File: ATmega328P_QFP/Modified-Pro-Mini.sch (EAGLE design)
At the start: 25 parts, among them Q1 8/16/20MHz, U1 ATMEGA328, U2 MIC5205

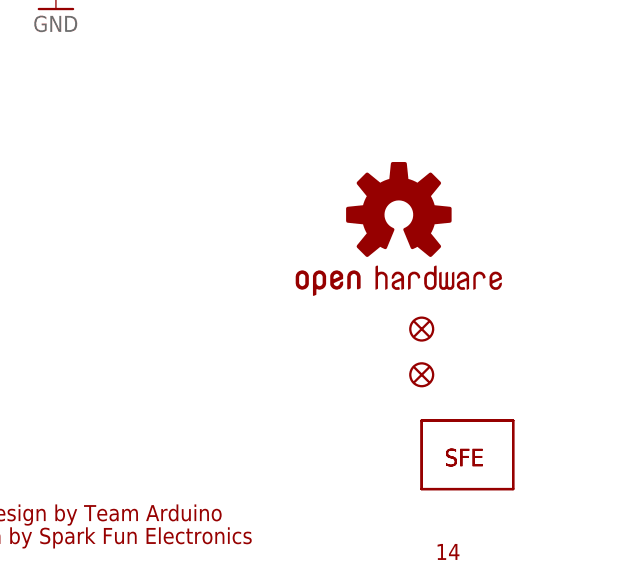
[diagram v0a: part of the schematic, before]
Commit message: updated silk
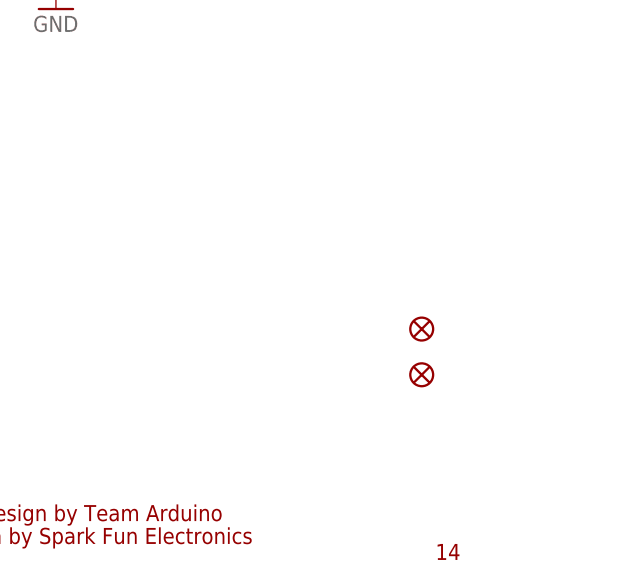
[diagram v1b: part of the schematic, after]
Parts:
- removed U$1: LOGO-SFESK, SparkFun:LOGO-SFESK
- removed U$11: LOGO-SFENEW, SparkFun:LOGO-SFENEW
- removed U$3: OSHW-LOGOS, SparkFun:OSHW-LOGOS
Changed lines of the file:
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@@
 <part name="D3" library="Testing" deviceset="LED" device="" value="Green"/>
 <part name="GND8" library="SparkFun" deviceset="GND" device=""/>
-<part name="U$11" library="SparkFun" deviceset="LOGO-SFE" device="NEW"/>
 <part name="U2" library="SparkFun" deviceset="V_REG_LDO" device="SMD" value="MIC5205"/>
 <part name="C19" library="SparkFun" deviceset="CAP_POL" device="1206" value="10uF"/>
@@
 <part name="JP6" library="SparkFun" deviceset="M12" device="PTH" value=""/>
 <part name="JP7" library="SparkFun" deviceset="M12" device="PTH" value=""/>
-<part name="U$1" library="SparkFun" deviceset="LOGO-SFE" device="SK"/>
 <part name="GND4" library="SparkFun" deviceset="GND" device=""/>
 <part name="JP2" library="SparkFun" deviceset="M02" device="PTH"/>
@@
 <part name="GND5" library="SparkFun" deviceset="GND" device=""/>
 <part name="JP1" library="SparkFun" deviceset="ARDUINO_SERIAL_PROGRAM" device="PTH" value="FTDI Basic"/>
-<part name="U$3" library="SparkFun" deviceset="OSHW-LOGO" device="S"/>
 <part name="R1" library="SparkFun" deviceset="RESISTOR" device="0603-RES"/>
 <part name="R3" library="SparkFun" deviceset="RESISTOR" device="0603-RES"/>
@@
 </instance>
 <instance part="GND8" gate="1" x="198.12" y="68.58"/>
-<instance part="U$11" gate="G$1" x="241.3" y="17.78"/>
 <instance part="U2" gate="G$1" x="45.72" y="157.48"/>
 <instance part="C19" gate="G$1" x="22.86" y="157.48"/>
@@
 <instance part="JP6" gate="G$1" x="106.68" y="83.82" rot="R180"/>
 <instance part="JP7" gate="G$1" x="55.88" y="86.36"/>
-<instance part="U$1" gate="G$1" x="241.3" y="17.78"/>
 <instance part="GND4" gate="1" x="134.62" y="119.38"/>
 <instance part="JP2" gate="G$1" x="73.66" y="43.18" rot="R180"/>
@@
 <instance part="GND5" gate="1" x="144.78" y="93.98"/>
 <instance part="JP1" gate="G$1" x="22.86" y="83.82"/>
-<instance part="U$3" gate="G$1" x="236.22" y="45.72"/>
 <instance part="R1" gate="G$1" x="223.52" y="152.4" rot="R90"/>
 <instance part="R3" gate="G$1" x="231.14" y="149.86" rot="R90"/>

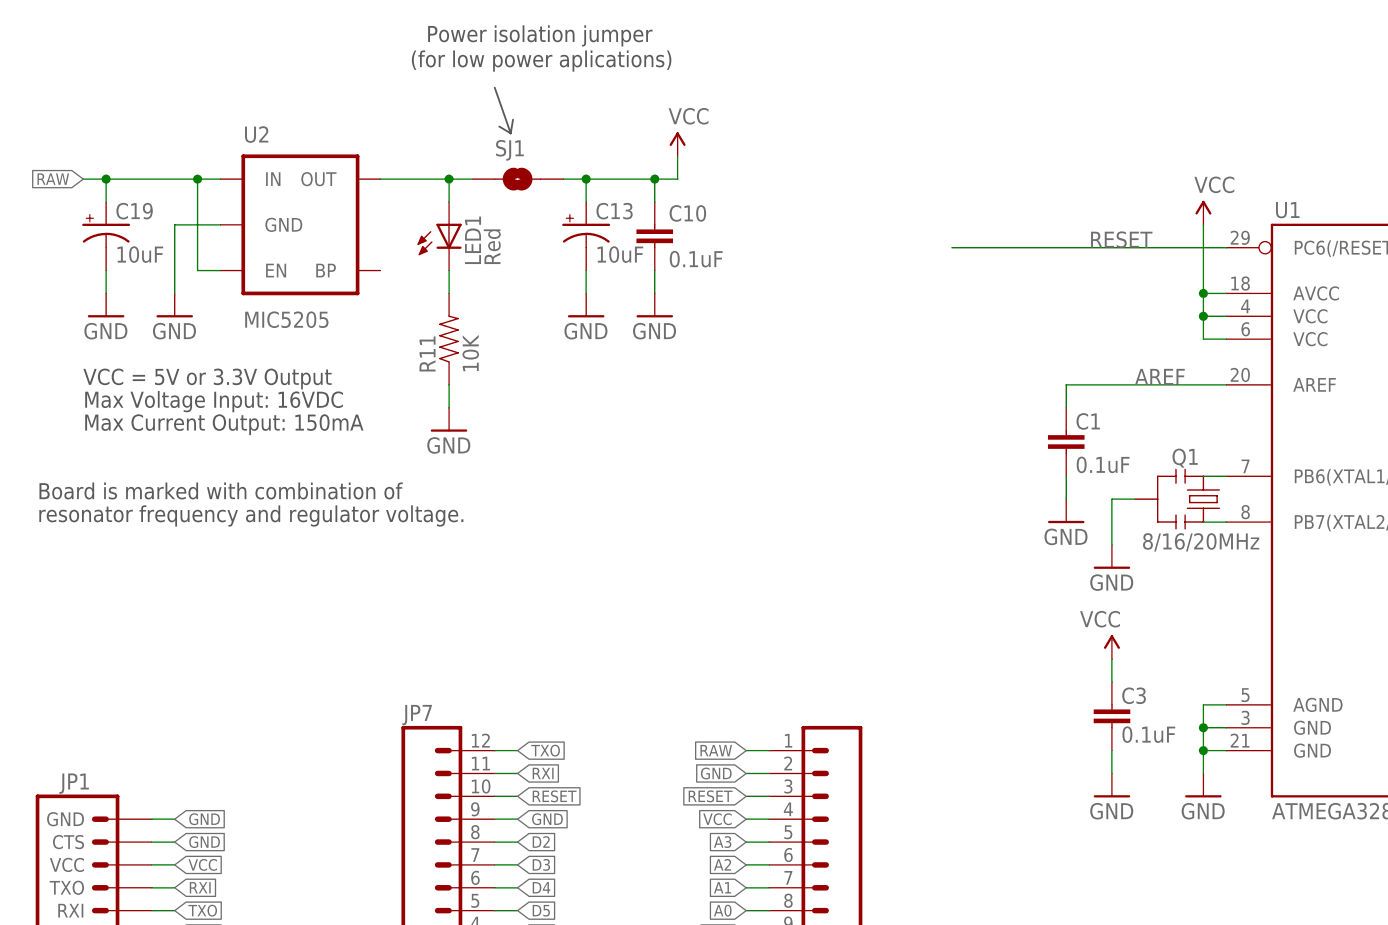
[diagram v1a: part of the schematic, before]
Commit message: removed power regulator
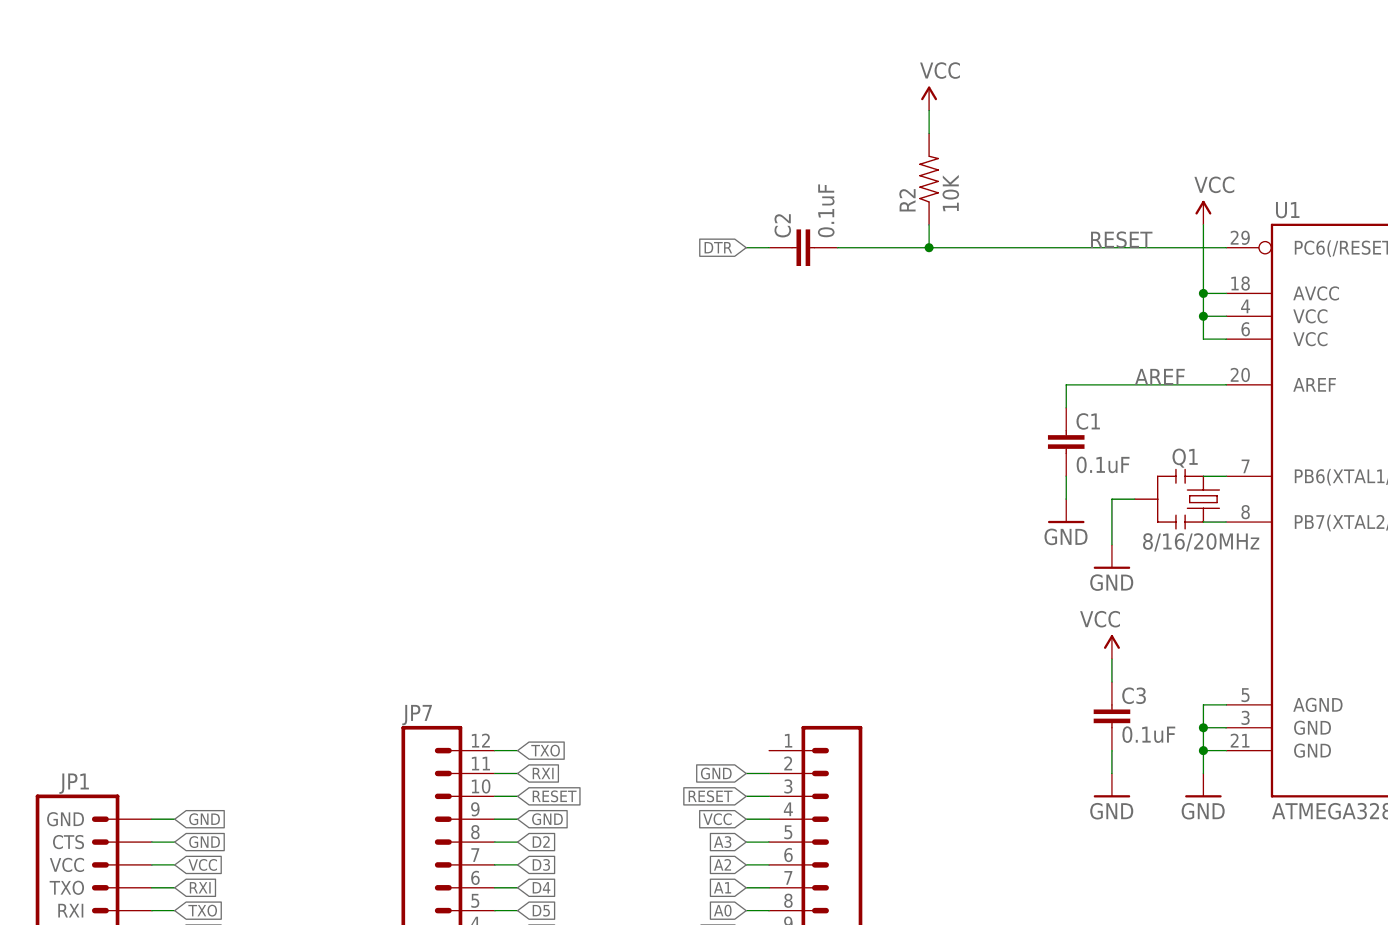
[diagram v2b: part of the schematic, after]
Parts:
- removed C10: 0.1uF, SparkFun:CAP0603-CAP
- removed C13, C19: 10uF, SparkFun:CAP_POL1206
- removed LED1: Red, Testing:LED
- removed R11: 10K, SparkFun:RESISTOR0603-RES
- removed SJ1: SOLDERJUMPERNC, SparkFun-Passives:SOLDERJUMPERNC
- removed U2: MIC5205, SparkFun:V_REG_LDOSMD
- added C2: 0.1uF, SparkFun:CAP0603-CAP
- added R2: 10K, SparkFun:RESISTOR0603-RES
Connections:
- removed net N$3: LED1.A, SJ1.1, U2.OUT
- removed net N$4: LED1.C, R11.2
- removed net RAW: C19.+, JP6.1, U2.EN, U2.IN
- net DTR: now also C2.2
- net GND: no longer C10.2, C13.-, C19.-, R11.1, U2.GND
- net RESET: now also C2.1, R2.1
- net VCC: now also R2.2; no longer C10.1, C13.+, SJ1.2
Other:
- note removed: "(for low power aplications)"
- note removed: "Board is marked with combination of"
- note removed: "Max Current Output: 150mA"
- note removed: "Max Voltage Input: 16VDC"
- note removed: "Power isolation jumper"
- note removed: "VCC = 5V or 3.3V Output"
- note removed: "resonator frequency and regulator voltage."

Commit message: changed raw pin to gnd
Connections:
- net GND: now also JP6.1
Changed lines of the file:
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@@
 <pinref part="JP6" gate="G$1" pin="2"/>
 <label x="93.98" y="96.52" size="1.27" layer="95" rot="R180" xref="yes"/>
+<pinref part="JP6" gate="G$1" pin="1"/>
+<wire x1="96.52" y1="99.06" x2="93.98" y2="99.06" width="0.1524" layer="91"/>
+<wire x1="93.98" y1="99.06" x2="93.98" y2="96.52" width="0.1524" layer="91"/>
 </segment>
 <segment>

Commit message: added decoupling cap
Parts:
- added C13: 10uF, SparkFun:CAP_POL1206
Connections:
- net GND: now also C13.-
- net VCC: now also C13.+
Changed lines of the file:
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@@
 <part name="P+11" library="SparkFun" deviceset="3.3V" device="" value="VCC"/>
 <part name="C2" library="SparkFun" deviceset="CAP" device="0603-CAP" value="0.1uF"/>
+<part name="C13" library="SparkFun" deviceset="CAP_POL" device="1206" value="10uF"/>
+<part name="GND25" library="SparkFun" deviceset="GND" device=""/>
 </parts>
 <sheets>
@@
 <attribute name="VALUE" x="103.759" y="155.956" size="1.778" layer="96" rot="R90"/>
 </instance>
+<instance part="C13" gate="G$1" x="93.98" y="132.08"/>
+<instance part="GND25" gate="1" x="93.98" y="121.92"/>
 </instances>
 <busses>
@@
 <label x="30.48" y="91.44" size="1.27" layer="95" xref="yes"/>
 </segment>
+<segment>
+<wire x1="93.98" y1="124.46" x2="93.98" y2="127" width="0.1524" layer="91"/>
+<pinref part="C13" gate="G$1" pin="-"/>
+<pinref part="GND25" gate="1" pin="GND"/>
+</segment>
 </net>
 <net name="AREF" class="0">
@@
 <pinref part="P+11" gate="G$1" pin="3.3V"/>
 </segment>
-</net>
+<segment>
+<pinref part="C13" gate="G$1" pin="+"/>
+<wire x1="93.98" y1="134.62" x2="93.98" y2="137.16" width="0.1524" layer="91"/>
+<label x="93.98" y="137.16" size="1.778" layer="95" rot="R90"/>
+</segment>
+</net>

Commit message: added decoupling cap
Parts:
- added C4: 0.1uF, SparkFun:CAP0603-CAP
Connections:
- net GND: now also C4.1
- net VCC: now also C4.2
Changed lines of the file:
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@@
 <part name="C13" library="SparkFun" deviceset="CAP_POL" device="1206" value="10uF"/>
 <part name="GND25" library="SparkFun" deviceset="GND" device=""/>
+<part name="C4" library="SparkFun" deviceset="CAP" device="0603-CAP" value="0.1uF"/>
+<part name="GND2" library="SparkFun" deviceset="GND" device=""/>
 </parts>
 <sheets>
@@
 <instance part="C13" gate="G$1" x="93.98" y="132.08"/>
 <instance part="GND25" gate="1" x="93.98" y="121.92"/>
+<instance part="C4" gate="G$1" x="104.14" y="132.08" smashed="yes" rot="R180">
+<attribute name="NAME" x="105.156" y="132.207" size="1.778" layer="95"/>
+<attribute name="VALUE" x="105.156" y="127.381" size="1.778" layer="96"/>
+</instance>
+<instance part="GND2" gate="1" x="104.14" y="121.92"/>
 </instances>
 <busses>
@@
 <pinref part="GND25" gate="1" pin="GND"/>
 </segment>
+<segment>
+<wire x1="104.14" y1="124.46" x2="104.14" y2="127" width="0.1524" layer="91"/>
+<pinref part="C4" gate="G$1" pin="1"/>
+<pinref part="GND2" gate="1" pin="GND"/>
+</segment>
 </net>
 <net name="AREF" class="0">
@@
 <label x="93.98" y="137.16" size="1.778" layer="95" rot="R90"/>
 </segment>
-</net>
+<segment>
+<pinref part="C4" gate="G$1" pin="2"/>
+<wire x1="104.14" y1="134.62" x2="104.14" y2="137.16" width="0.1524" layer="91"/>
+<label x="104.14" y="137.16" size="1.778" layer="95" rot="R90"/>
+</segment>
+</net>

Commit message: Prepare silkscreen layers for OSH Park printing (#4)
* Fix typo in bPlace layer
* Remove fiducials
* Cleared the tNames layer
* Slight adjustments to prevent text from overlapping copper
* got rid of kink in TXO line
* moved via slightly
* bottom silk tweak
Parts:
- removed JP5, JP8: FIDUCIALUFIDUCIAL, SparkFun:FIDUCIALUFIDUCIAL
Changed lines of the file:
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@@
 <part name="P+2" library="SparkFun" deviceset="3.3V" device="" value="VCC"/>
 <part name="P+3" library="SparkFun" deviceset="3.3V" device="" value="VCC"/>
-<part name="JP5" library="SparkFun" deviceset="FIDUCIAL" device="UFIDUCIAL"/>
-<part name="JP8" library="SparkFun" deviceset="FIDUCIAL" device="UFIDUCIAL"/>
 <part name="JP3" library="SparkFun" deviceset="M02" device="PTH"/>
 <part name="Q1" library="Testing" deviceset="RESONATOR" device="1:1" value="8/16/20MHz"/>
@@
 <instance part="P+2" gate="G$1" x="223.52" y="160.02"/>
 <instance part="P+3" gate="G$1" x="231.14" y="160.02"/>
-<instance part="JP5" gate="G$1" x="238.76" y="27.94"/>
-<instance part="JP8" gate="G$1" x="238.76" y="33.02"/>
 <instance part="JP3" gate="G$1" x="99.06" y="43.18" rot="R180"/>
 <instance part="Q1" gate="G$1" x="144.78" y="127" smashed="yes" rot="R270">

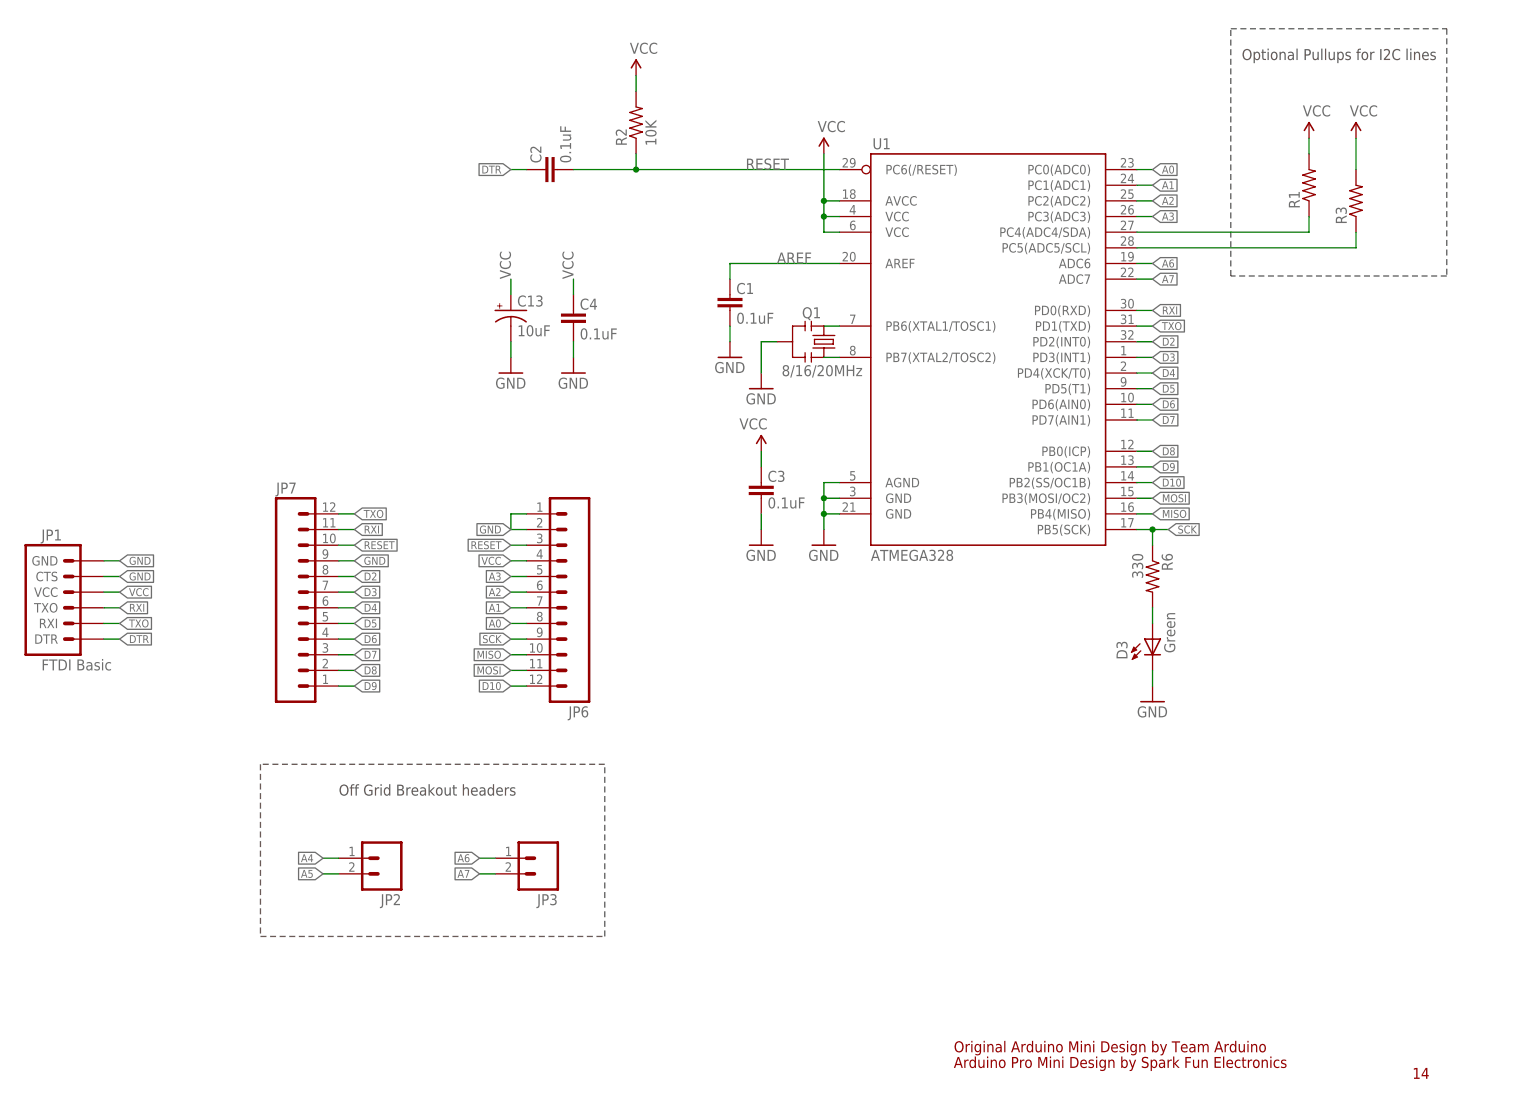
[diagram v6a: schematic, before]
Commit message: New board design: - larger footprint by the ICD requirements (no holes) - removed headers - added DF12 connector footprint
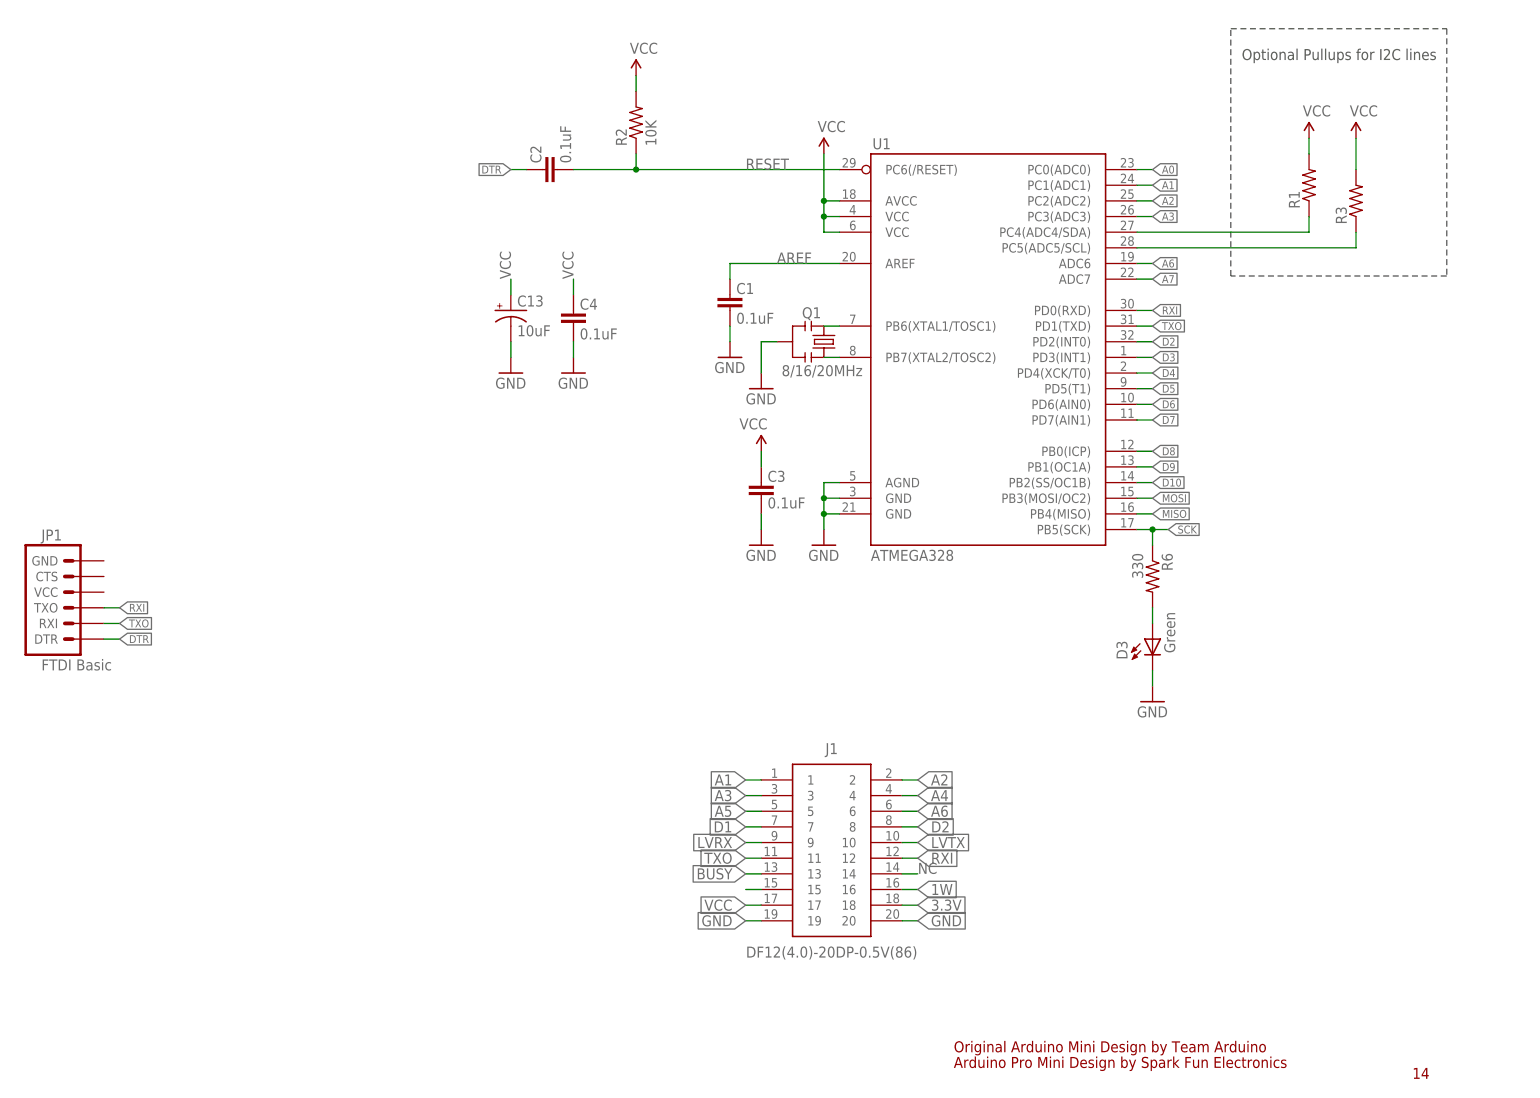
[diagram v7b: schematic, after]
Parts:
- removed JP2, JP3: (no value), SparkFun:M02PTH
- removed JP6, JP7: M12PTH, SparkFun:M12PTH
- added J1: DF12(4.0)-20DP-0.5V(86), DF12(4.0)-20DP-0.5V(86):DF12(4.0)-20DP-0.5V(86)
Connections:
- new net 1W: J1.16
- new net 3.3V: J1.18
- new net BUSY: J1.13
- new net D1: J1.7
- new net LVRX: J1.9
- new net LVTX: J1.10
- new net N$9: J1.15
- new net NC: J1.14
- net A0: no longer JP6.8
- net A1: now also J1.1; no longer JP6.7
- net A2: now also J1.2; no longer JP6.6
- net A3: now also J1.3; no longer JP6.5
- net A4: now also J1.4; no longer JP2.1
- net A5: now also J1.5; no longer JP2.2
- net A6: now also J1.6; no longer JP3.1
- net A7: no longer JP3.2
- net D10: no longer JP6.12
- net D2: now also J1.8; no longer JP7.8
- net D3: no longer JP7.7
- net D4: no longer JP7.6
- net D5: no longer JP7.5
- net D6: no longer JP7.4
- net D7: no longer JP7.3
- net D8: no longer JP7.2
- net D9: no longer JP7.1
- net GND: now also J1.19, J1.20; no longer JP1.CTS, JP1.GND, JP6.1, JP6.2, JP7.9
- net MISO: no longer JP6.10
- net MOSI: no longer JP6.11
- net RESET: no longer JP6.3, JP7.10
- net RXI: now also J1.12; no longer JP7.11
- net SCK: no longer JP6.9
- net TXO: now also J1.11; no longer JP7.12
- net VCC: now also J1.17; no longer JP1.VCC, JP6.4
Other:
- note removed: "Off Grid Breakout headers"
